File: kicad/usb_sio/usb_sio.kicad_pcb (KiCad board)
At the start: 2 copper layers, 38.1 x 114.3 mm, 24 parts, among them CON1 USB, P1 Z80_BUS_PINS, P2 IO_BUS_PINS, P3 CONN_02X05, U1 MCP2200, U2 68B50, U3 74HCT04, U4 1.8432MHz, Y1 12MHz

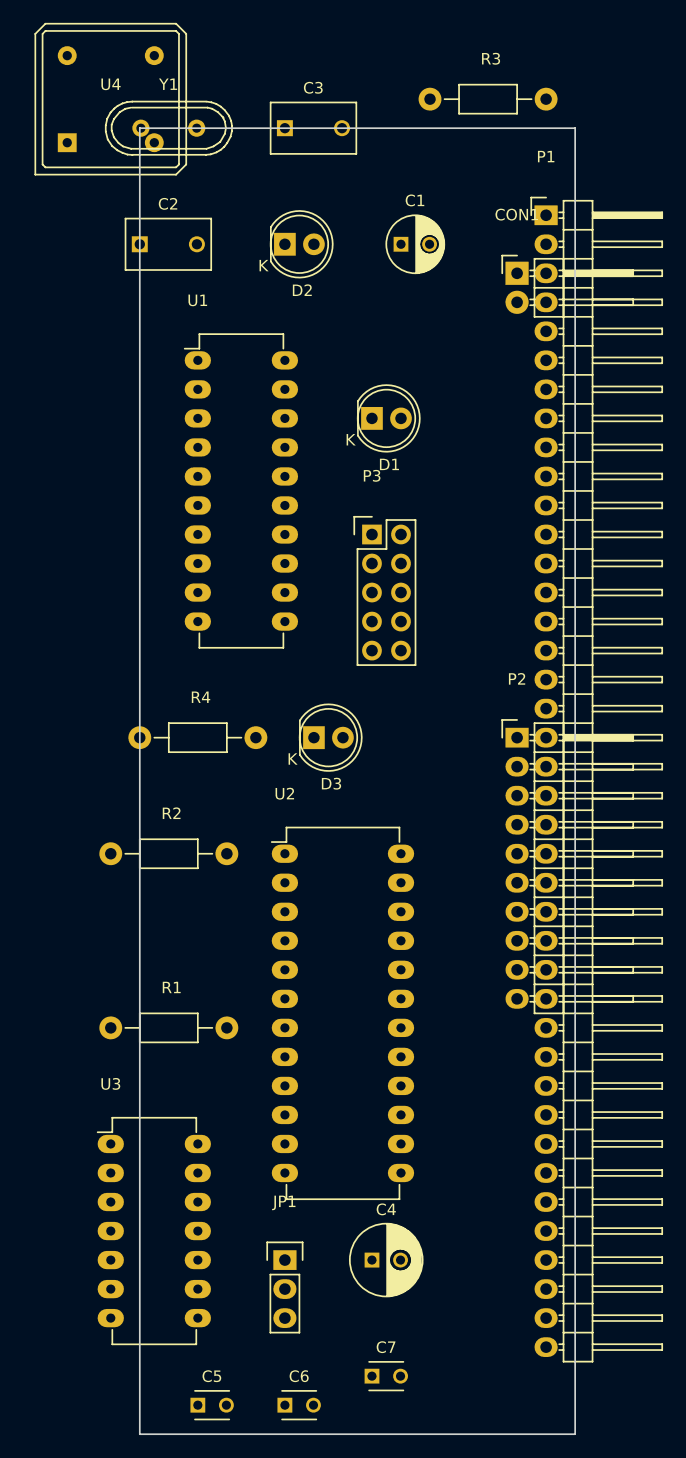
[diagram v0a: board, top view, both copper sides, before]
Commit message: Added major work to SIO board.
Coming along nicely. Had to use SOIC for the USB to serial converter. :(
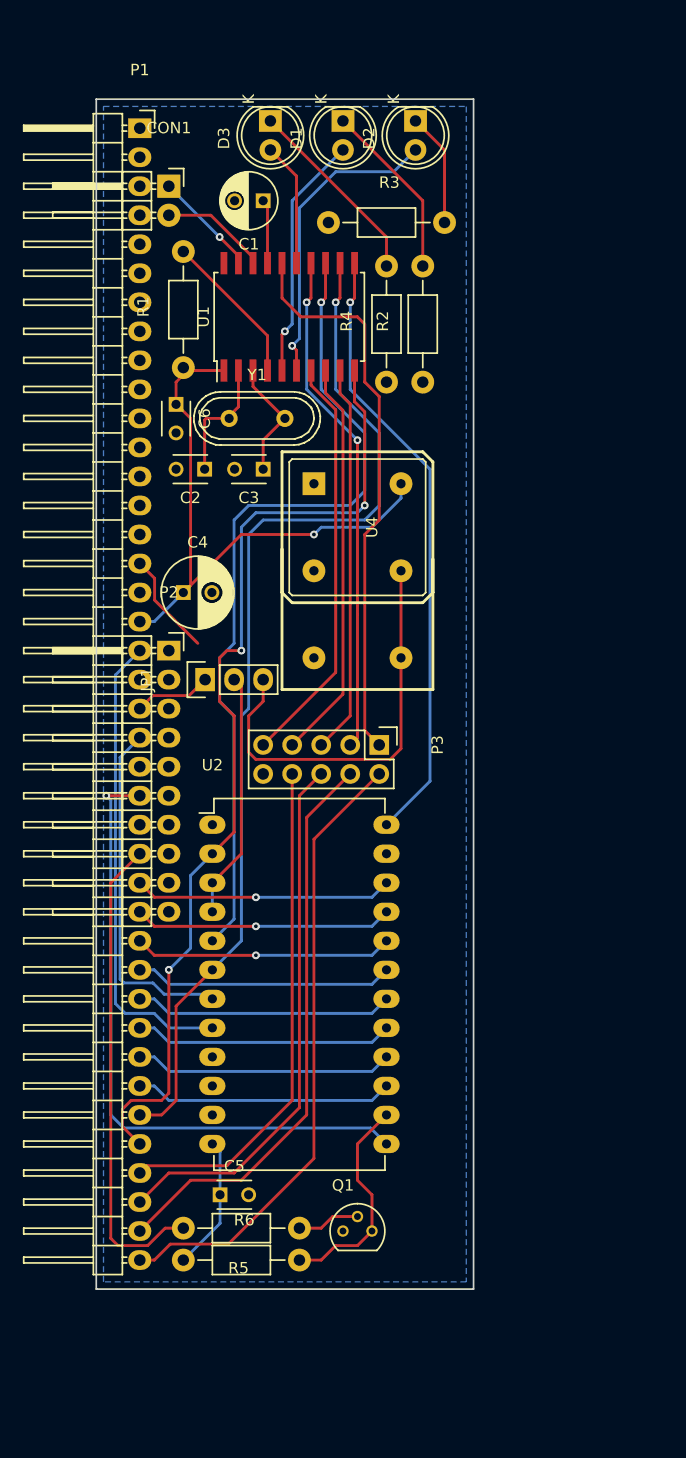
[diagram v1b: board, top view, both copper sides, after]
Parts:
- removed C7: 100nF, Capacitors_ThroughHole:C_Disc_D3_P2.5
- removed U3: 74HCT04, Housings_DIP:DIP-14_W7.62mm_LongPads
- added Q1: Q_NPN_EBC, TO_SOT_Packages_THT:TO-92_Molded_Narrow, F.Cu at (81.3, 134.6)
- added R5: 10K, Resistors_ThroughHole:Resistor_Horizontal_RM10mm, F.Cu at (77.5, 134.4)
- added R6: 2K2, Resistors_ThroughHole:Resistor_Horizontal_RM10mm, F.Cu at (67.3, 137.2)
- C2, C3: footprint Capacitors_ThroughHole:C_Disc_D7.5_P5 -> Capacitors_ThroughHole:C_Disc_D3_P2.5
- CON1: footprint Pin_Headers:Pin_Header_Angled_1x02 -> nrc2016:Pin_Header_Angled_1x02_nrc2016
- P1: footprint Pin_Headers:Pin_Header_Angled_1x40 -> nrc2016:Pin_Header_Angled_1x40_nrc2016
- P2: footprint Pin_Headers:Pin_Header_Angled_1x10 -> nrc2016:Pin_Header_Angled_1x10_nrc2016
- U1: footprint Housings_DIP:DIP-20_W7.62mm_LongPads -> Housings_SOIC:SOIC-20W_7.5x12.8mm_Pitch1.27mm
- U2: footprint Housings_DIP:DIP-24_W10.16mm_LongPads -> Housings_DIP:DIP-24_W15.24mm_LongPads
- U4: footprint Oscillators:OSC_DIP8 -> nrc2016:OSC_MULTIPACKAGE_DIP
- moved C6 88.1 mm to (66.7, 62.3), turned to 270 degrees
- moved C4 60.7 mm to (67.3, 78.7)
- moved R1 58.1 mm to (67.3, 59.1), turned to 90 degrees
- moved D3 54.1 mm to (74.9, 37.5), turned to 270 degrees
- moved JP1 51.3 mm to (69.2, 86.4), turned to 90 degrees
- moved R2 49.5 mm to (88.3, 60.3), turned to 90 degrees
- moved P1 45.1 mm to (54.6, 38.1)
- moved U4 43.2 mm to (82.5, 73.0), turned to 270 degrees
- moved CON1 40.1 mm to (57.1, 43.2)
- moved R4 37.9 mm to (85.1, 60.3), turned to 90 degrees
- moved P2 35.1 mm to (62.2, 83.8)
- moved C3 29.9 mm to (74.3, 67.9), turned to 180 degrees
- moved Y1 26.5 mm to (73.8, 63.5)
- moved D1 26.2 mm to (81.3, 37.5), turned to 270 degrees
- moved C2 20.5 mm to (69.2, 67.9), turned to 180 degrees
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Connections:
- JP1 pad 3: (no net) -> Net-(JP1-Pad3)
- P3 pad 2: /S1 -> /S4
- P3 pad 4: /S2 -> /S3
- P3 pad 6: /S3 -> /S2
- P3 pad 8: /S4 -> /S1
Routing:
- net /TX: track 0.00 -> 91.3 mm, vias 0 -> 1
- net /RX: track 0.00 -> 86.0 mm, vias 0 -> 3
- net Net-(U1-Pad13): track 0.00 -> 72.8 mm, vias 0 -> 1
- net VCC: track 0.00 -> 64.2 mm, vias 0 -> 1
- net /~WR: track 0.00 -> 56.2 mm, vias 0 -> 1
- net /S4: track 0.00 -> 54.9 mm
- net Net-(U1-Pad11): track 0.00 -> 53.8 mm, vias 0 -> 1
- net /S3: track 0.00 -> 50.2 mm
- net /GP0: track 0.00 -> 49.6 mm
- net /S2: track 0.00 -> 47.4 mm
- net /S1: track 0.00 -> 44.5 mm
- net /GP2: track 0.00 -> 44.4 mm, vias 0 -> 2
- net /~IORQ: track 0.00 -> 42.0 mm
- net /~M1: track 0.00 -> 41.1 mm
- net Net-(JP1-Pad3): track 0.00 -> 36.4 mm
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- added copper zone on B.Cu, net GND
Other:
- board size 38.1 x 114.3 mm -> 33 x 104.1 mm
- net class Default: clearance 0.2 -> 0.1524; trace_width 0.25 -> 0.254; via_dia 0.6 -> 0.6858; via_drill 0.4 -> 0.3302
- rule trace_clearance: 0.2 -> 0.1524
- rule trace_min: 0.2 -> 0.1524
- rule via_min_drill: 0.3 -> 0.3302
- rule via_min_size: 0.4 -> 0.6858

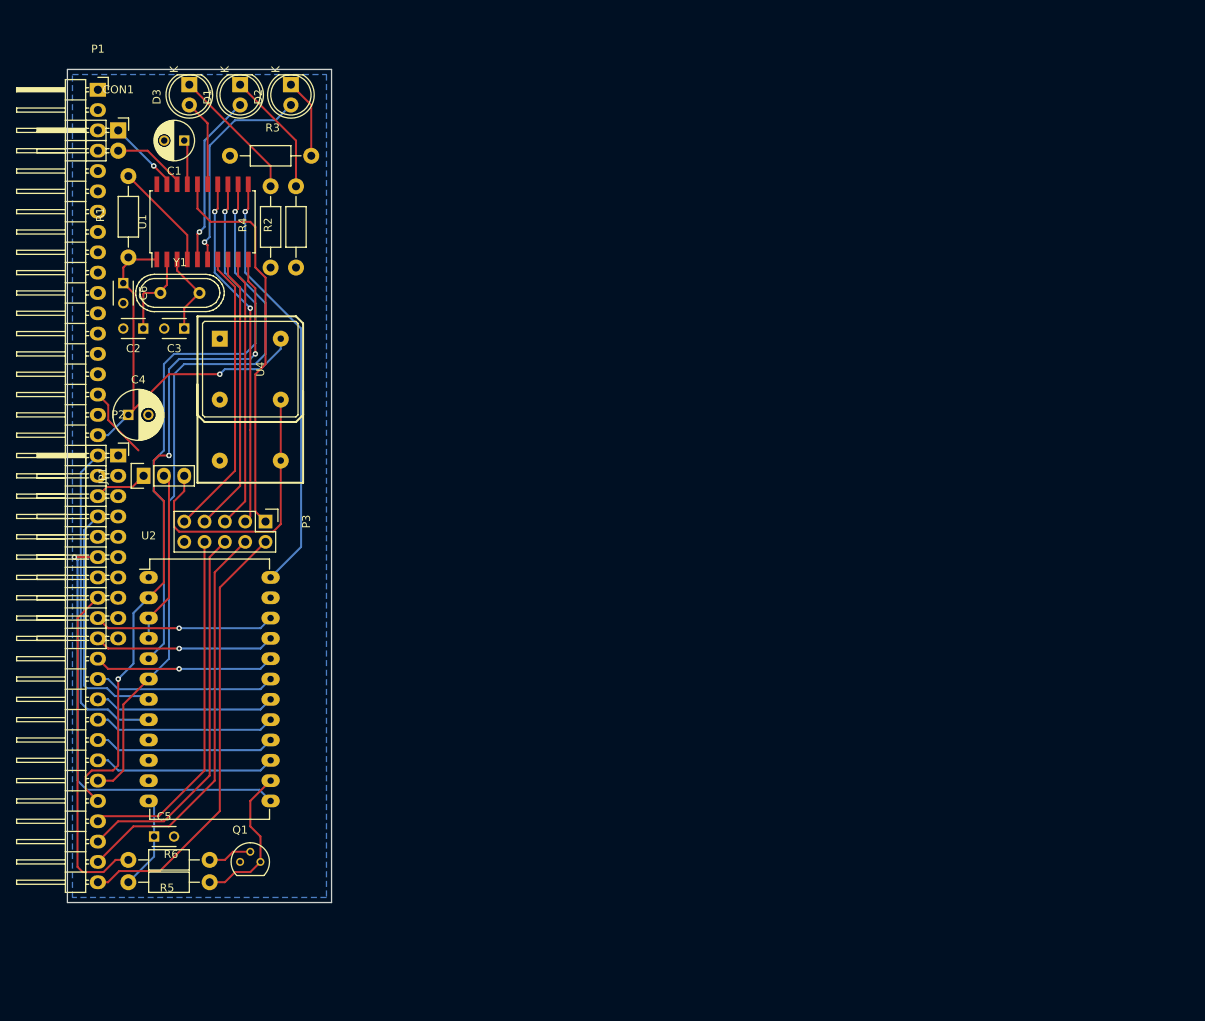
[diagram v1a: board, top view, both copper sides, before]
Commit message: Update to the SIO board, layout complete!
Added headers for selecting the IOSEL to use, added logo, silkscreen
legends etc.
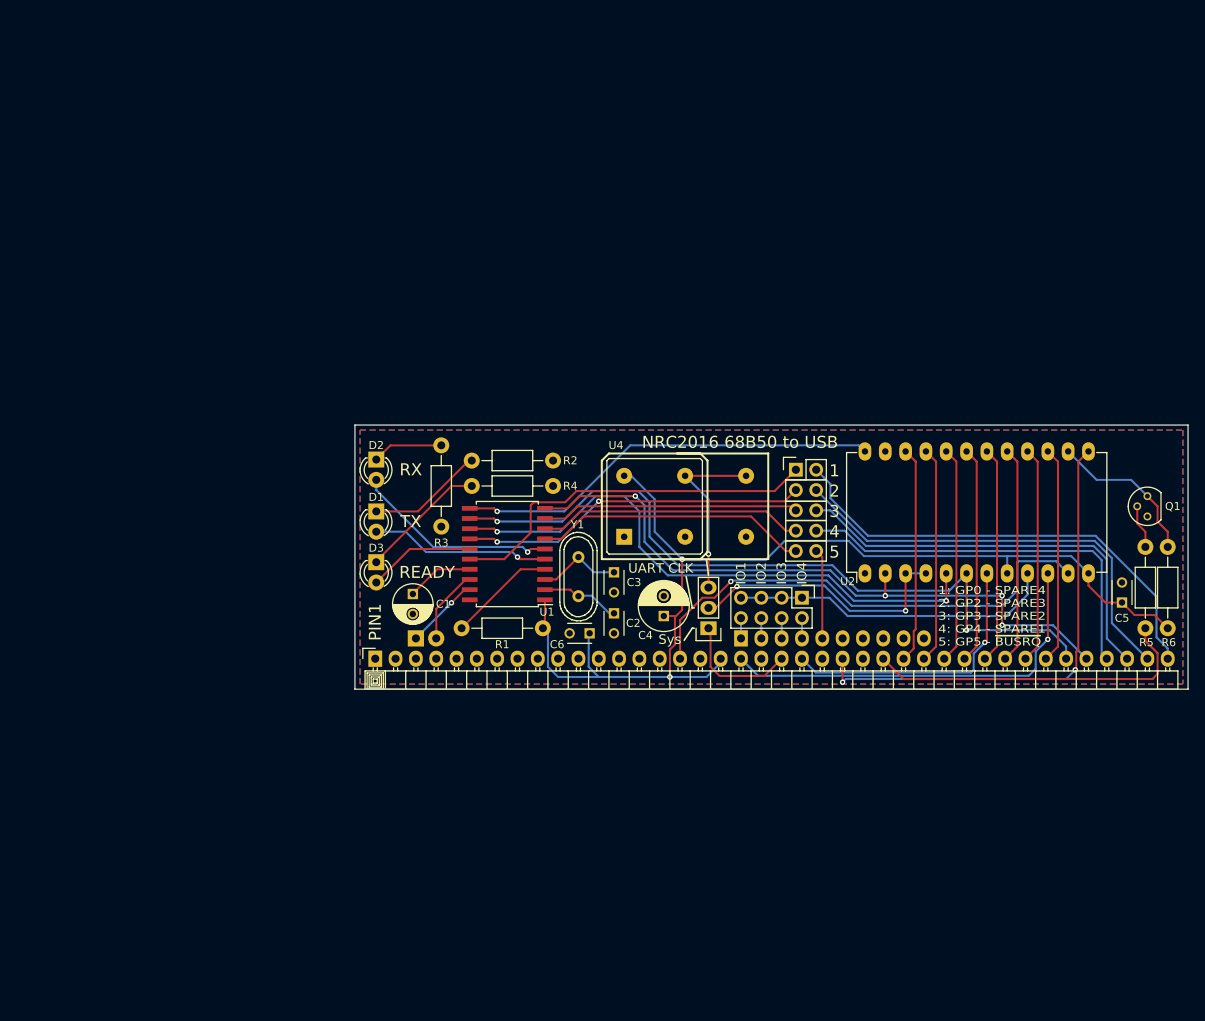
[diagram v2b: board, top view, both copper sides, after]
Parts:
- added LOGO1: BackLogo, nrc2016_logo:nrc2016_top_logo_1600, B.Cu at (173.7, 90.7)
- added P4: CONN_02X04, Pin_Headers:Pin_Header_Straight_2x04, F.Cu at (151.5, 101.6)
- D1, D2, D3: footprint LEDs:LED-5MM -> LEDs:LED-3MM
- moved R6 133.7 mm to (197.2, 105.4), turned to 90 degrees
- moved C5 124.5 mm to (191.5, 102.2), turned to 90 degrees
- moved R5 123.3 mm to (194.4, 95.2), turned to 270 degrees
- moved Q1 121.4 mm to (194.7, 91.4), turned to 90 degrees
- moved P1 91.1 mm to (98.2, 118.1), turned to 90 degrees
- moved U2 89.5 mm to (159.4, 98.6), turned to 90 degrees
- moved P2 85.9 mm to (143.9, 110.5), turned to 90 degrees
- moved CON1 85.8 mm to (103.3, 115.6), turned to 90 degrees
- moved JP1 73.1 mm to (139.8, 105.4), turned to 180 degrees
- moved C6 72.9 mm to (125.0, 106.0), turned to 180 degrees
- moved C4 71.5 mm to (134.2, 103.9), turned to 90 degrees
- moved R1 69.5 mm to (119.1, 105.4), turned to 180 degrees
- moved C2 68.8 mm to (128.0, 103.5), turned to 270 degrees
- moved P3 66.6 mm to (150.7, 85.6), turned to 0 degrees
- moved D3 64.1 mm to (98.3, 97.2)
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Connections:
- P2 pad 1: /IOSEL -> Net-(P2-Pad1)
- P2 pad 2: (no net) -> Net-(P2-Pad2)
- P2 pad 3: (no net) -> Net-(P2-Pad3)
- P2 pad 4: (no net) -> Net-(P2-Pad4)
- U2 pad 8: /~M1 -> VCC
- U2 pad 9: /IOSEL -> /~IOSEL
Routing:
- net VCC: track 64.2 -> 138.3 mm, vias 1 -> 2
- net /A0: track 9.09 -> 61.7 mm, vias 0 -> 1
- net /~IOSEL: track 0.00 -> 40.5 mm
- net Net-(JP1-Pad3): track 36.4 -> 22.8 mm, vias 0 -> 1
- net Net-(JP1-Pad2): track 21.6 -> 34.3 mm, vias 0 -> 2
- net /~BUSRQ: track 0.00 -> 11.2 mm
- net /~M1: track 41.1 -> 50.6 mm, vias 0 -> 1
- net /~CLK: track 6.77 -> 15.2 mm
- net /S1: track 44.5 -> 49.8 mm
- net /S3: track 50.2 -> 55.4 mm
- net /S2: track 47.4 -> 52.3 mm
- net /D4: track 22.6 -> 27.1 mm
- net /D5: track 22.6 -> 27.1 mm
- net /D0: track 22.6 -> 27.1 mm, vias 1 -> 0
- net /D2: track 22.6 -> 27.1 mm, vias 1 -> 0
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- added copper zone on F.Cu, net GND
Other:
- board size 33 x 104.1 mm -> 104.1 x 33 mm
- board text added: "1"
- board text added: "1: GP0 - SPARE4 2: GP2 - SPARE3 3: GP3 - SPARE2 4: GP4 - SPARE1 5: GP5 - ~BUSRQ"
- board text added: "2"
- board text added: "3"
- board text added: "4"
- board text added: "5"
- board text added: "By Alan Garfield & Niels Moseley"
- board text added: "IO1"
- board text added: "IO2"
- board text added: "IO3"
- board text added: "IO4"
- board text added: "NRC2016 68B50 to USB"
- board text added: "PIN1"
- board text added: "READY"
- board text added: "RX"
- board text added: "Sys"
- board text added: "TX"
- board text added: "UART CLK"

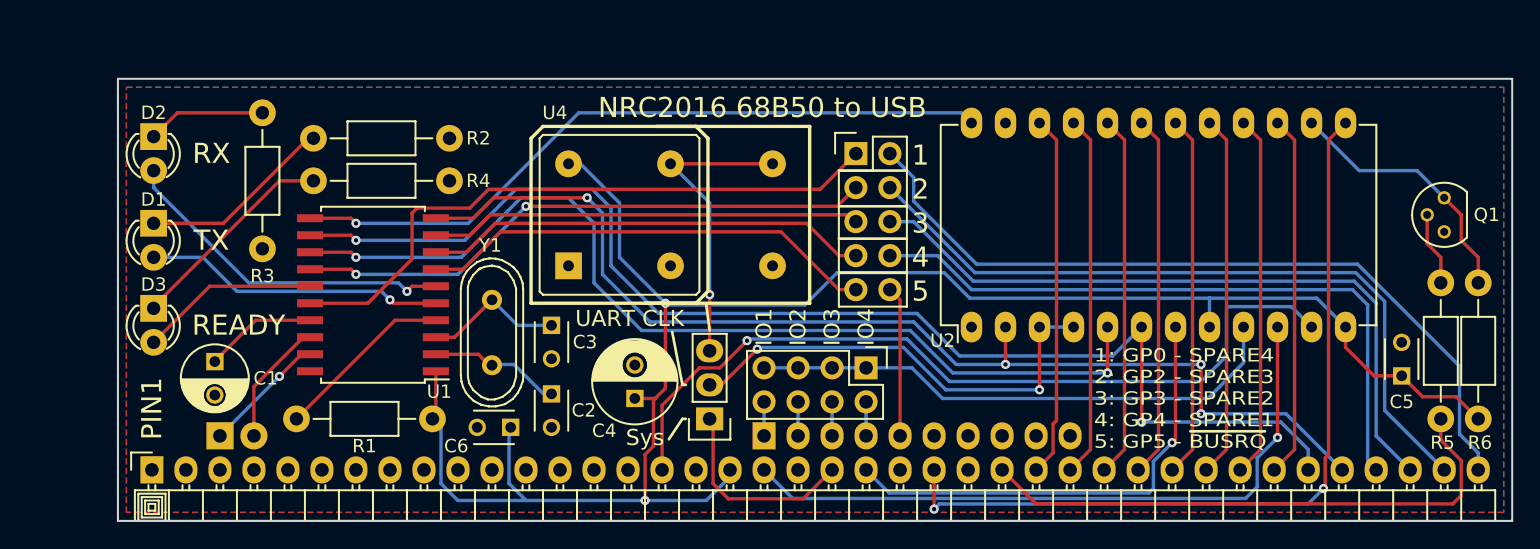
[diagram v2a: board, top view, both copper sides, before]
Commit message: Banked RAM board completed
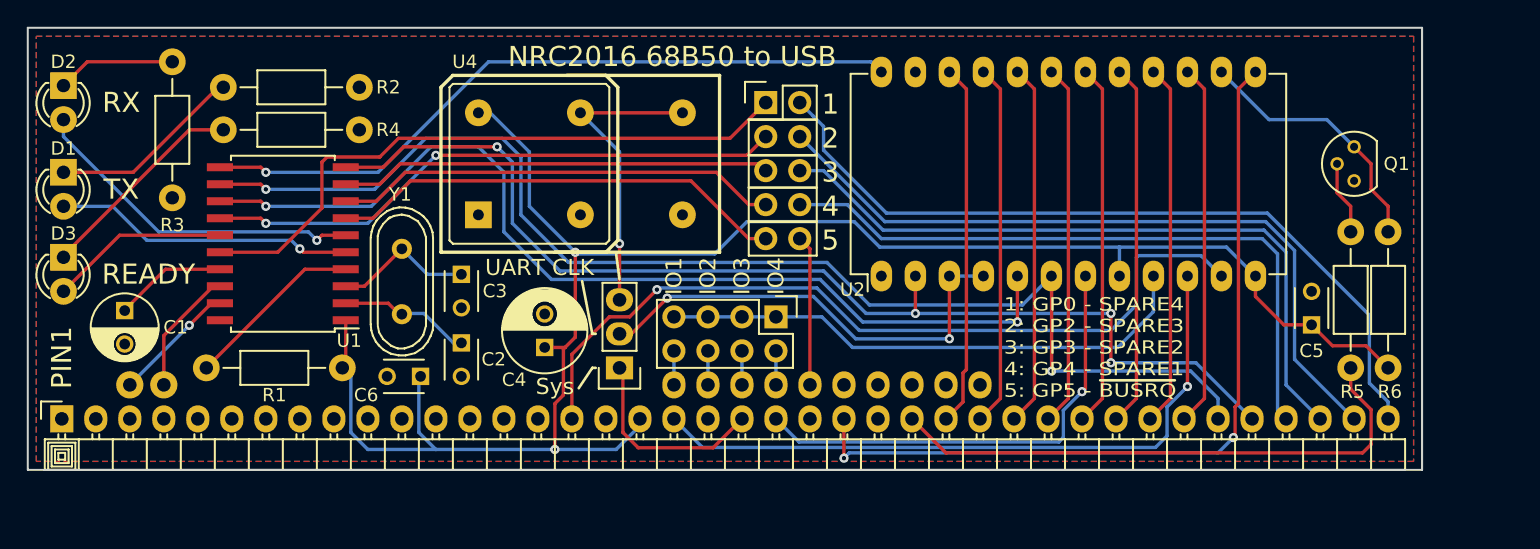
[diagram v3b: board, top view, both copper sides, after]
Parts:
- CON1: footprint nrc2016:Pin_Header_Angled_1x02_nrc2016 -> Pin_Header_Angled_1x02_nrc2016
- P2: footprint nrc2016:Pin_Header_Angled_1x10_nrc2016 -> Pin_Header_Angled_1x10_nrc2016
- moved R5 7.73 mm to (187.7, 91.4)
- moved C1 7.73 mm to (96.1, 97.3)
- moved C4 7.73 mm to (127.5, 100.1)
- moved C6 7.73 mm to (118.2, 102.2)
- moved D1 7.73 mm to (91.6, 87.0)
- moved D2 7.73 mm to (91.6, 80.5)
- moved D3 7.73 mm to (91.6, 93.3)
- moved P1 7.73 mm to (91.4, 114.3)
- moved R1 7.73 mm to (112.4, 101.6)
- moved U4 7.73 mm to (126.4, 86.4)
- moved CON1 7.73 mm to (96.5, 111.8)
- moved R3 7.73 mm to (99.7, 88.9)
- moved C2 7.73 mm to (121.3, 99.7)
- moved C3 7.73 mm to (121.3, 94.6)
- moved JP1 7.73 mm to (133.1, 101.6)
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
